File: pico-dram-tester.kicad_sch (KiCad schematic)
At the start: 44 parts, among them J1 TFT 4383, J2 mrd_114_ips_lcd_8p, Q1 2N3906, SW1 RotaryEncoder_Switch, SW2 BACK, U1 PICO2, U2 4116, U3 4132, U4 4164/41128/41256, U5 4416/4464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

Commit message: Layout corrections
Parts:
- removed Q1: 2N3906, Package_TO_SOT_THT:TO-92_Inline_Wide, symbol Transistor_BJT:2N3906
- added Q1: XP9561GI, Package_TO_SOT_THT:TO-220-3_Vertical, symbol Transistor_FET:IRF9540N
- R5: value 4.7K -> 100
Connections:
- net +5V: now also Q1.2 (D)
- net VCC: now also Q1.3 (S)
- net at R4.2, R5.1: now also Q1.1 (G)
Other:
- moved on the sheet: TP6
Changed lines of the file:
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@@
 	(symbol
 		(lib_id "Connector:TestPoint")
-		(at 38.1 41.91 0)
+		(at 31.75 31.75 0)
 		(unit 1)
 		(exclude_from_sim no)
@@
 		(fields_autoplaced yes)
 		(property "Reference" "TP6"
-			(at 40.64 37.3379 0)
+			(at 34.29 27.1779 0)
 			(effects
 				(font
@@
 		)
 		(property "Value" "GND"
-			(at 40.64 39.8779 0)
+			(at 34.29 29.7179 0)
 			(effects
 				(font
@@
 		)
 		(property "Footprint" "TestPoint:TestPoint_Keystone_5005-5009_Compact"
-			(at 43.18 41.91 0)
+			(at 36.83 31.75 0)
 			(effects
 				(font
@@
 		)
 		(property "Datasheet" "~"
-			(at 43.18 41.91 0)
+			(at 36.83 31.75 0)
 			(effects
 				(font
@@
 		)
 		(property "Description" "test point"
-			(at 38.1 41.91 0)
+			(at 31.75 31.75 0)
 			(effects
 				(font
@@
 	)
 	(symbol
-		(lib_id "Transistor_BJT:2N3906")
-		(at 38.1 57.15 270)
-		(mirror x)
-		(unit 1)
-		(exclude_from_sim no)
-		(in_bom yes)
-		(on_board yes)
-		(dnp no)
-		(fields_autoplaced yes)
-		(property "Reference" "Q1"
-			(at 38.1 48.26 90)
-			(effects
-				(font
-					(size 1.27 1.27)
-				)
-			)
-		)
-		(property "Value" "2N3906"
-			(at 38.1 50.8 90)
-			(effects
-				(font
-					(size 1.27 1.27)
-				)
-			)
-		)
-		(property "Footprint" "Package_TO_SOT_THT:TO-92_Inline_Wide"
-			(at 36.195 52.07 0)
-			(effects
-				(font
-					(size 1.27 1.27)
-					(italic yes)
-				)
-				(justify left)
-				(hide yes)
-			)
-		)
-		(property "Datasheet" "https://www.onsemi.com/pub/Collateral/2N3906-D.PDF"
-			(at 38.1 57.15 0)
-			(effects
-				(font
-					(size 1.27 1.27)
-				)
-				(justify left)
-				(hide yes)
-			)
-		)
-		(property "Description" "-0.2A Ic, -40V Vce, Small Signal PNP Transistor, TO-92"
-			(at 38.1 57.15 0)
-			(effects
-				(font
-					(size 1.27 1.27)
-				)
-				(hide yes)
-			)
-		)
-		(pin "1"
-		)
-		(pin "2"
-		)
-		(pin "3"
-		)
-		(instances
-			(project ""
-				(path "/497e03e6-87e1-44a4-a7c3-4726983a3602"
-					(reference "Q1")
-					(unit 1)
-				)
-			)
-		)
-	)
-	(symbol
 		(lib_id "power:GND")
 		(at 173.99 62.23 0)
@@
 	)
 	(symbol
+		(lib_id "Transistor_FET:IRF9540N")
+		(at 38.1 57.15 270)
+		(mirror x)
+		(unit 1)
+		(exclude_from_sim no)
+		(in_bom yes)
+		(on_board yes)
+		(dnp no)
+		(property "Reference" "Q1"
+			(at 38.1 48.26 90)
+			(effects
+				(font
+					(size 1.27 1.27)
+				)
+			)
+		)
+		(property "Value" "XP9561GI"
+			(at 38.1 50.8 90)
+			(effects
+				(font
+					(size 1.27 1.27)
+				)
+			)
+		)
+		(property "Footprint" "Package_TO_SOT_THT:TO-220-3_Vertical"
+			(at 36.195 52.07 0)
+			(effects
+				(font
+					(size 1.27 1.27)
+					(italic yes)
+				)
+				(justify left)
+				(hide yes)
+			)
+		)
+		(property "Datasheet" ""
+			(at 34.29 52.07 0)
+			(effects
+				(font
+					(size 1.27 1.27)
+				)
+				(justify left)
+				(hide yes)
+			)
+		)
+		(property "Description" ""
+			(at 38.1 57.15 0)
+			(effects
+				(font
+					(size 1.27 1.27)
+				)
+				(hide yes)
+			)
+		)
+		(property "Mouser" "603-XP9561GI"
+			(at 38.1 57.15 0)
+			(effects
+				(font
+					(size 1.27 1.27)
+				)
+				(hide yes)
+			)
+		)
+		(pin "1"
+		)
+		(pin "3"
+		)
+		(pin "2"
+		)
+		(instances
+			(project ""
+				(path "/497e03e6-87e1-44a4-a7c3-4726983a3602"
+					(reference "Q1")
+					(unit 1)
+				)
+			)
+		)
+	)
+	(symbol
 		(lib_id "power:GND")
 		(at 26.67 105.41 0)
@@
 	(symbol
 		(lib_id "power:GND")
-		(at 38.1 41.91 0)
+		(at 31.75 31.75 0)
 		(unit 1)
 		(exclude_from_sim no)
@@
 		(fields_autoplaced yes)
 		(property "Reference" "#PWR02"
-			(at 38.1 48.26 0)
+			(at 31.75 38.1 0)
 			(effects
 				(font
@@
 		)
 		(property "Value" "GND"
-			(at 38.1 46.99 0)
+			(at 31.75 36.83 0)
 			(effects
 				(font
@@
 		)
 		(property "Footprint" ""
-			(at 38.1 41.91 0)
+			(at 31.75 31.75 0)
 			(effects
 				(font
@@
 		)
 		(property "Datasheet" ""
-			(at 38.1 41.91 0)
+			(at 31.75 31.75 0)
 			(effects
 				(font
@@
 		)
 		(property "Description" "Power symbol creates a global label with name \"GND\" , ground"
-			(at 38.1 41.91 0)
+			(at 31.75 31.75 0)
 			(effects
 				(font
@@
 			)
 		)
-		(property "Value" "4.7K"
+		(property "Value" "100"
 			(at 49.53 71.12 90)
 			(effects

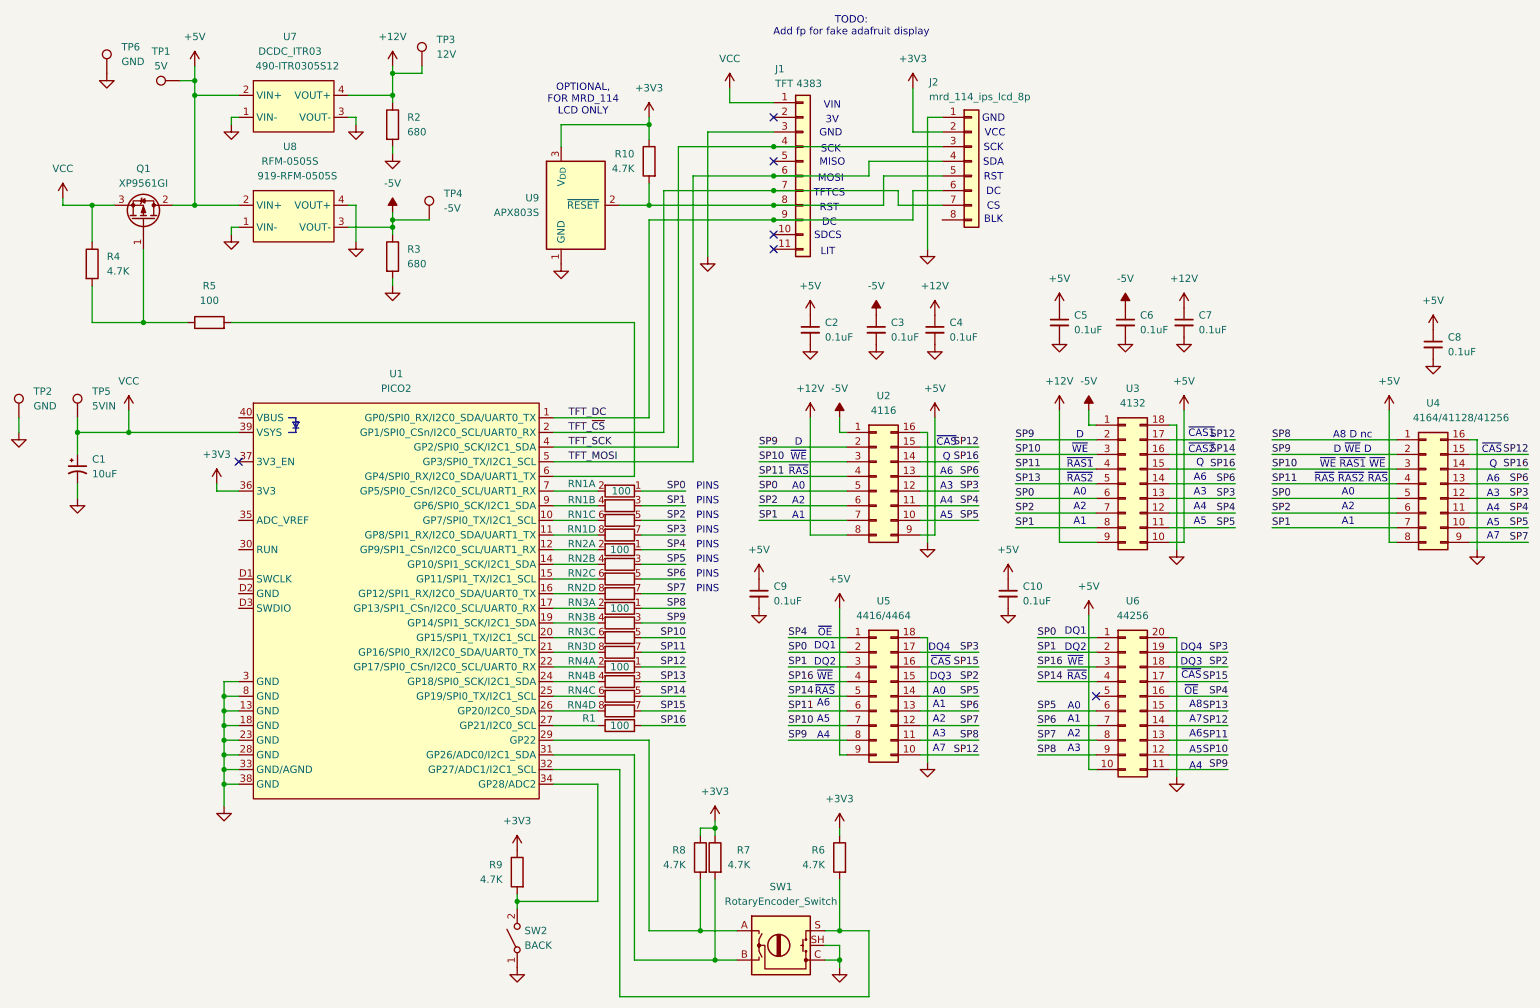
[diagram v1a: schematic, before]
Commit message: Add readme and new fab package
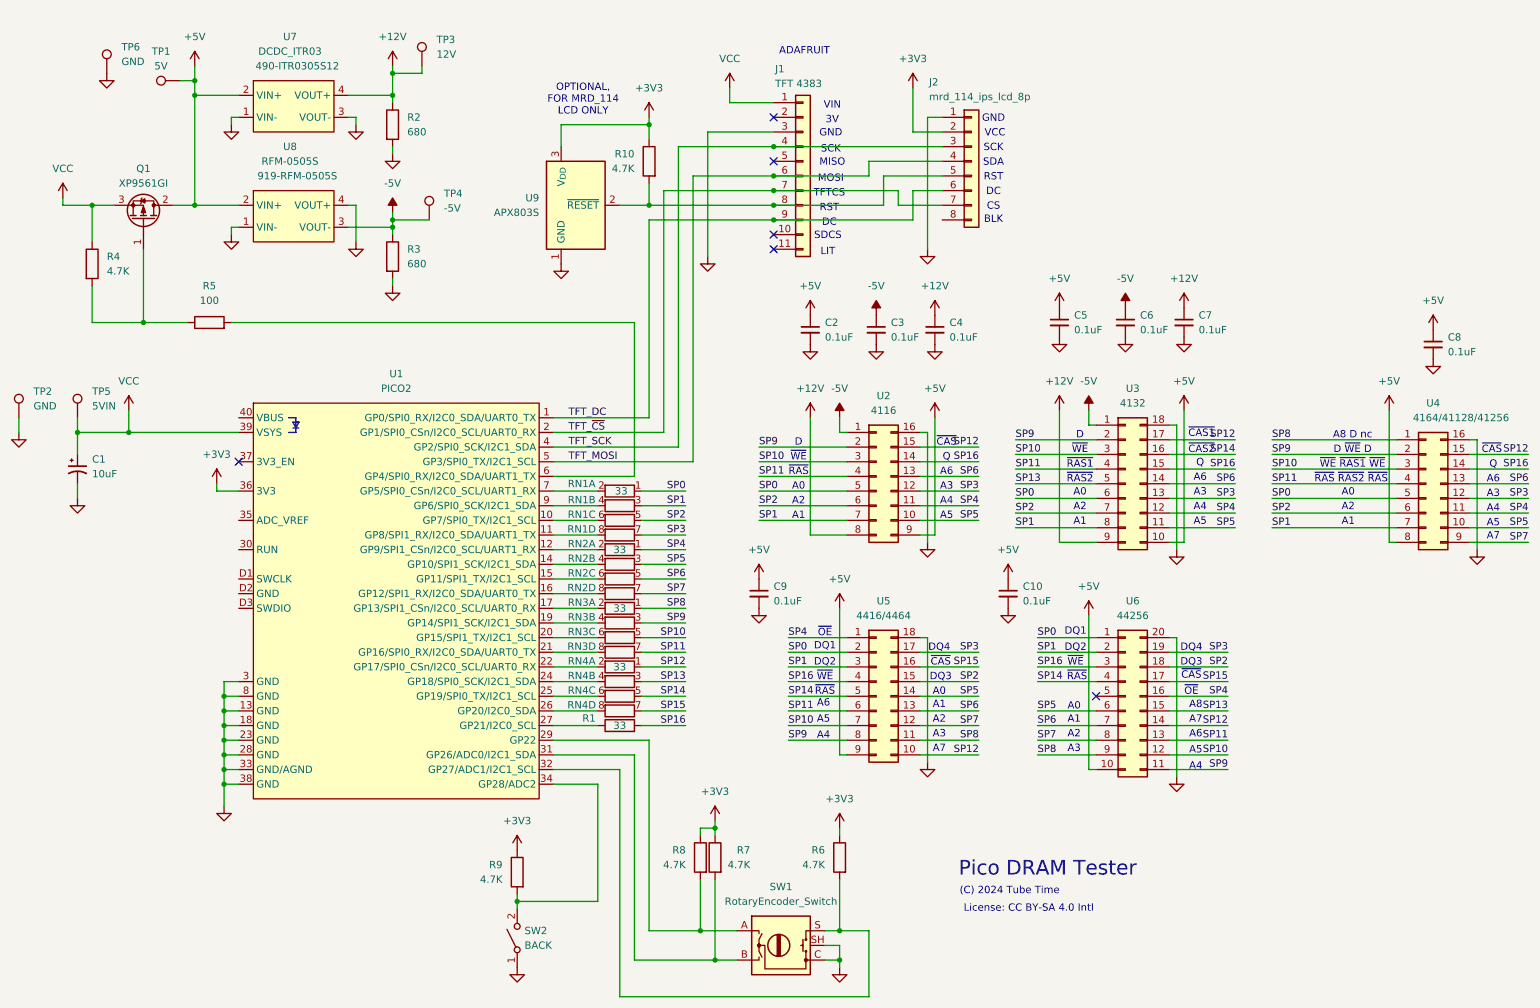
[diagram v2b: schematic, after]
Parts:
- R1, RN1, RN2, RN3, RN4: value 100 -> 33
- TP1, TP5: Mouser (none) -> 534-5005
- TP2, TP6: Mouser (none) -> 534-5006
- TP3: Mouser (none) -> 534-5009
- TP4: Mouser (none) -> 534-5007
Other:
- note added: "(C) 2024 Tube Time"
- note added: "ADAFRUIT"
- note added: "License: CC BY-SA 4.0 Intl"
- note added: "Pico DRAM Tester"
- note removed: "PINS"
- note removed: "TODO: Add fp for fake adafruit display"
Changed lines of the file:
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@@
 		)
 	)
-	(text "PINS"
-		(exclude_from_sim no)
-		(at 135.89 118.618 0)
-		(effects
-			(font
-				(size 1.27 1.27)
-			)
-		)
-	)
 	(text "DC"
 		(exclude_from_sim no)
@@
 		)
 	)
-	(text "A1"
+	(text "ADAFRUIT"
 		(exclude_from_sim no)
-		(at 199.39 143.764 0)
+		(at 152.654 27.94 0)
 		(effects
 			(font
@@
 		)
 	)
-	(text "PINS"
+	(text "A1"
 		(exclude_from_sim no)
-		(at 135.89 116.078 0)
+		(at 199.39 143.764 0)
 		(effects
 			(font
@@
 		)
 	)
-	(text "PINS"
-		(exclude_from_sim no)
-		(at 135.89 105.918 0)
-		(effects
-			(font
-				(size 1.27 1.27)
-			)
-		)
-	)
 	(text "GND"
 		(exclude_from_sim no)
@@
 		)
 	)
+	(text "License: CC BY-SA 4.0 Intl"
+		(exclude_from_sim no)
+		(at 191.516 176.53 0)
+		(effects
+			(font
+				(size 1.27 1.27)
+			)
+		)
+	)
 	(text "A0"
 		(exclude_from_sim no)
@@
 		)
 	)
+	(text "(C) 2024 Tube Time"
+		(exclude_from_sim no)
+		(at 188.214 173.482 0)
+		(effects
+			(font
+				(size 1.27 1.27)
+			)
+		)
+	)
 	(text "A5"
 		(exclude_from_sim no)
@@
 		)
 	)
-	(text "TODO:\nAdd fp for fake adafruit display"
-		(exclude_from_sim no)
-		(at 160.782 23.622 0)
-		(effects
-			(font
-				(size 1.27 1.27)
-			)
-		)
-	)
 	(text "SDA"
 		(exclude_from_sim no)
@@
 		)
 	)
-	(text "PINS"
-		(exclude_from_sim no)
-		(at 135.89 103.378 0)
-		(effects
-			(font
-				(size 1.27 1.27)
-			)
-		)
-	)
-	(text "PINS"
-		(exclude_from_sim no)
-		(at 135.89 110.998 0)
-		(effects
-			(font
-				(size 1.27 1.27)
-			)
-		)
-	)
-	(text "PINS"
+	(text "A2"
 		(exclude_from_sim no)
-		(at 135.89 108.458 0)
+		(at 176.022 143.764 0)
 		(effects
 			(font
@@
 		)
 	)
-	(text "A2"
+	(text "Pico DRAM Tester"
 		(exclude_from_sim no)
-		(at 176.022 143.764 0)
+		(at 194.818 169.672 0)
 		(effects
 			(font
-				(size 1.27 1.27)
+				(size 2.54 2.54)
 			)
 		)
@@
 		)
 	)
-	(text "PINS"
-		(exclude_from_sim no)
-		(at 135.89 113.538 0)
-		(effects
-			(font
-				(size 1.27 1.27)
-			)
-		)
-	)
 	(text "A0"
 		(exclude_from_sim no)
@@
 		)
 	)
-	(text "PINS"
-		(exclude_from_sim no)
-		(at 135.89 121.158 0)
-		(effects
-			(font
-				(size 1.27 1.27)
-			)
-		)
-	)
 	(text "A5"
 		(exclude_from_sim no)
@@
 			)
 		)
-		(property "Value" "100"
+		(property "Value" "33"
 			(at 120.65 123.19 90)
 			(effects
@@
 			)
 		)
+		(property "Mouser" "534-5006"
+			(at 31.75 31.75 0)
+			(effects
+				(font
+					(size 1.27 1.27)
+				)
+				(hide yes)
+			)
+		)
 		(pin "1"
 		)
@@
 			)
 		)
-		(property "Value" "100"
+		(property "Value" "33"
 			(at 120.65 125.73 90)
 			(effects
@@
 			)
 		)
-		(property "Value" "100"
+		(property "Value" "33"
 			(at 120.65 144.78 90)
 			(effects
@@
 			)
 		)
-		(property "Value" "100"
+		(property "Value" "33"
 			(at 120.904 104.14 90)
 			(effects
@@
 			)
 		)
-		(property "Value" "100"
+		(property "Value" "33"
 			(at 120.65 105.41 90)
 			(effects
@@
 			)
 		)
-		(property "Value" "100"
+		(property "Value" "33"
 			(at 120.65 138.43 90)
 			(effects
@@
 			)
 		)
-		(property "Value" "100"
+		(property "Value" "33"
 			(at 120.65 102.87 90)
 			(effects
@@
 			)
 		)
-		(property "Value" "100"
+		(property "Value" "33"
 			(at 120.65 107.95 90)
 			(effects
@@
 			)
 		)
+		(property "Mouser" "534-5005"
+			(at 44.45 33.02 0)
+			(effects
+				(font
+					(size 1.27 1.27)
+				)
+				(hide yes)
+			)
+		)
 		(pin "1"
 		)
@@
 			)
 		)
-		(property "Value" "100"
+		(property "Value" "33"
 			(at 120.65 124.46 90)
 			(effects
@@
 			)
 		)
+		(property "Mouser" "534-5007"
+			(at 87.63 57.15 0)
+			(effects
+				(font
+					(size 1.27 1.27)
+				)
+				(hide yes)
+			)
+		)
 		(pin "1"
 		)
@@
 			)
 		)
+		(property "Mouser" "534-5009"
+			(at 86.36 30.48 0)
+			(effects
+				(font
+					(size 1.27 1.27)
+				)
+				(hide yes)
+			)
+		)
 		(pin "1"
 		)
@@
 			)
 		)
-		(property "Value" "100"
+		(property "Value" "33"
 			(at 120.65 114.3 90)
 			(effects
@@
 			)
 		)
+		(property "Mouser" "534-5006"
+			(at 16.51 91.44 0)
+			(effects
+				(font
+					(size 1.27 1.27)
+				)
+				(hide yes)
+			)
+		)
 		(pin "1"
 		)
@@
 			)
 		)
-		(property "Value" "100"
+		(property "Value" "33"
 			(at 120.65 134.62 90)
 			(effects
@@
 			)
 		)
-		(property "Value" "100"
+		(property "Value" "33"
 			(at 120.65 135.89 90)
 			(effects
@@
 			)
 		)
+		(property "Mouser" "534-5005"
+			(at 26.67 91.44 0)
+			(effects
+				(font
+					(size 1.27 1.27)
+				)
+				(hide yes)
+			)
+		)
 		(pin "1"
 		)
@@
 			)
 		)
-		(property "Value" "100"
+		(property "Value" "33"
 			(at 120.65 115.57 90)
 			(effects
@@
 			)
 		)
-		(property "Value" "100"
+		(property "Value" "33"
 			(at 120.65 113.03 90)
 			(effects
@@
 			)
 		)
-		(property "Value" "100"
+		(property "Value" "33"
 			(at 120.65 133.35 90)
 			(effects
@@
 			)
 		)
-		(property "Value" "100"
+		(property "Value" "33"
 			(at 120.65 128.27 90)
 			(effects
@@
 			)
 		)
-		(property "Value" "100"
+		(property "Value" "33"
 			(at 120.65 118.11 90)
 			(effects

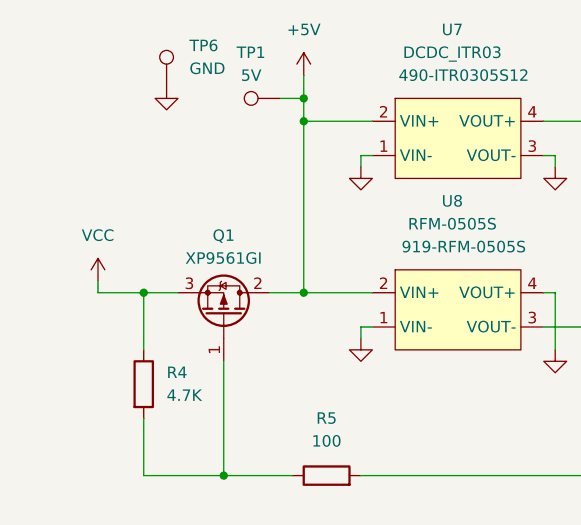
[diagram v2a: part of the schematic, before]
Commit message: Update MOSFET Q1, fix R1 part number
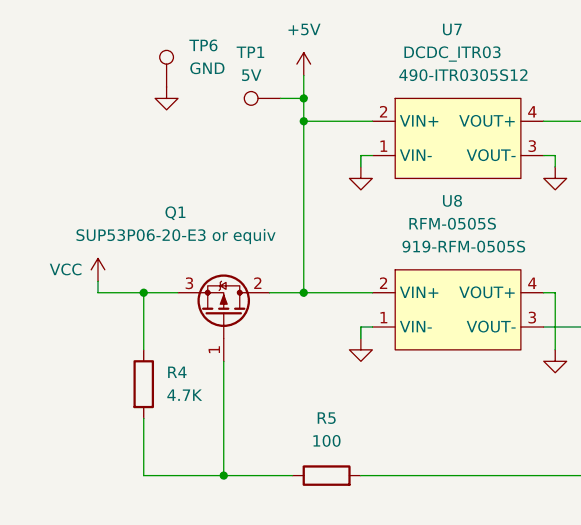
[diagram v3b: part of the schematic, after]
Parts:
- C1: Mouser (none) -> 667-ECA-1VM100
- C10, C2, C3, C4, C5, C6, C7, C8, C9: Mouser (none) -> 80-C322C104M5U
- Q1: value XP9561GI -> SUP53P06-20-E3 or equiv; Mouser 603-XP9561GI -> 781-SUP53P06-20-E3
- R1: Mouser (none) -> 594-MBB02070C3309FCT
- R10, R4, R6, R7, R8, R9: Mouser (none) -> 594-MBB02070C4701FCT
- R2, R3: Mouser (none) -> 594-MBB02070C6800FCT
- R5: Mouser (none) -> 594-MBB02070C1000FCT
- RN1, RN2, RN3, RN4: Mouser (none) -> 652-4608X-2LF-33
- U1: Mouser (none) -> 358-SC1631

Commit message: DCJack and Generic Encoder
Added DC Barrel Jack. Added Configuration Jumper pads to use the common Generic Encoder
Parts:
- removed TP6: GND, TestPoint:TestPoint_Keystone_5005-5009_Compact, symbol Connector:TestPoint
- added J3: 5V DC Jack, Connector_BarrelJack:BarrelJack_Horizontal, symbol Connector:Barrel_Jack_Switch
- added JP1: EncoderCFG, Jumper:SolderJumper-3_P1.3mm_Open_Pad1.0x1.5mm, symbol Jumper:SolderJumper_3_Open
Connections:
- net SP9 is gone; now on net +5V: RN3.3 (R2.1), U2.2 (Pin_2), U3.2 (Pin_2), U4.2 (Pin_2), U5.8 (Pin_8), U6.11 (Pin_11)
- net GND: now also J3.2, JP1.3 (B)
- net VCC: now also J3.1
- net at R7.2, SW1.B, U1.31 (GP26/ADC0/I2C1_SDA): now also JP1.1 (A)
- new net: JP1.2 (C), SW1.O
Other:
- moved on the sheet: R6, R7, R8, R9, SW2
